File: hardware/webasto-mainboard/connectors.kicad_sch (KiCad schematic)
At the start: 5 parts

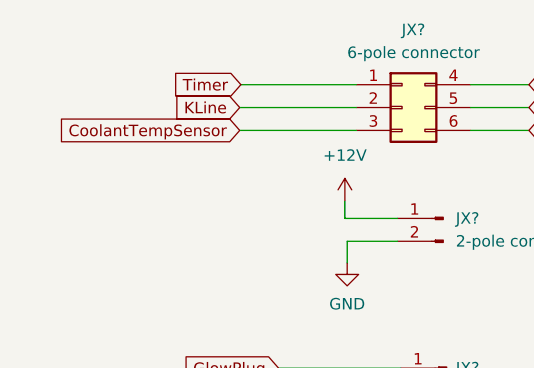
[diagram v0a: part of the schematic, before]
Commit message: Update schematics.  Had a better idea.
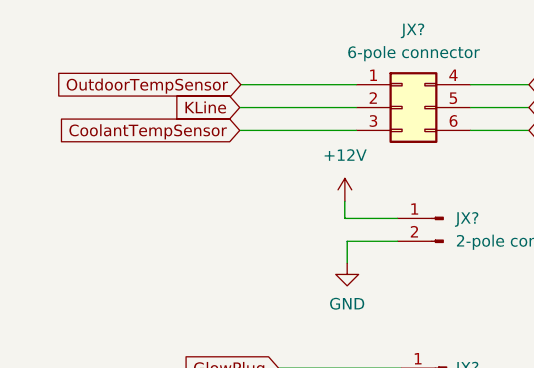
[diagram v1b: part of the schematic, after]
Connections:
- net Timer renamed OutdoorTempSensor
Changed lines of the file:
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@@
     )
   )
-  (global_label "Timer" (shape input) (at 127.508 58.166 180) (fields_autoplaced)
+  (global_label "OutdoorTempSensor" (shape input) (at 127.508 58.166 180) (fields_autoplaced)
     (effects (font (size 1.27 1.27)) (justify right))
-    (property "Intersheet References" "${INTERSHEET_REFS}" (id 0) (at 119.9544 58.0866 0)
+    (property "Intersheet References" "${INTERSHEET_REFS}" (id 0) (at 106.3473 58.0866 0)
       (effects (font (size 1.27 1.27)) (justify right) hide)
     )

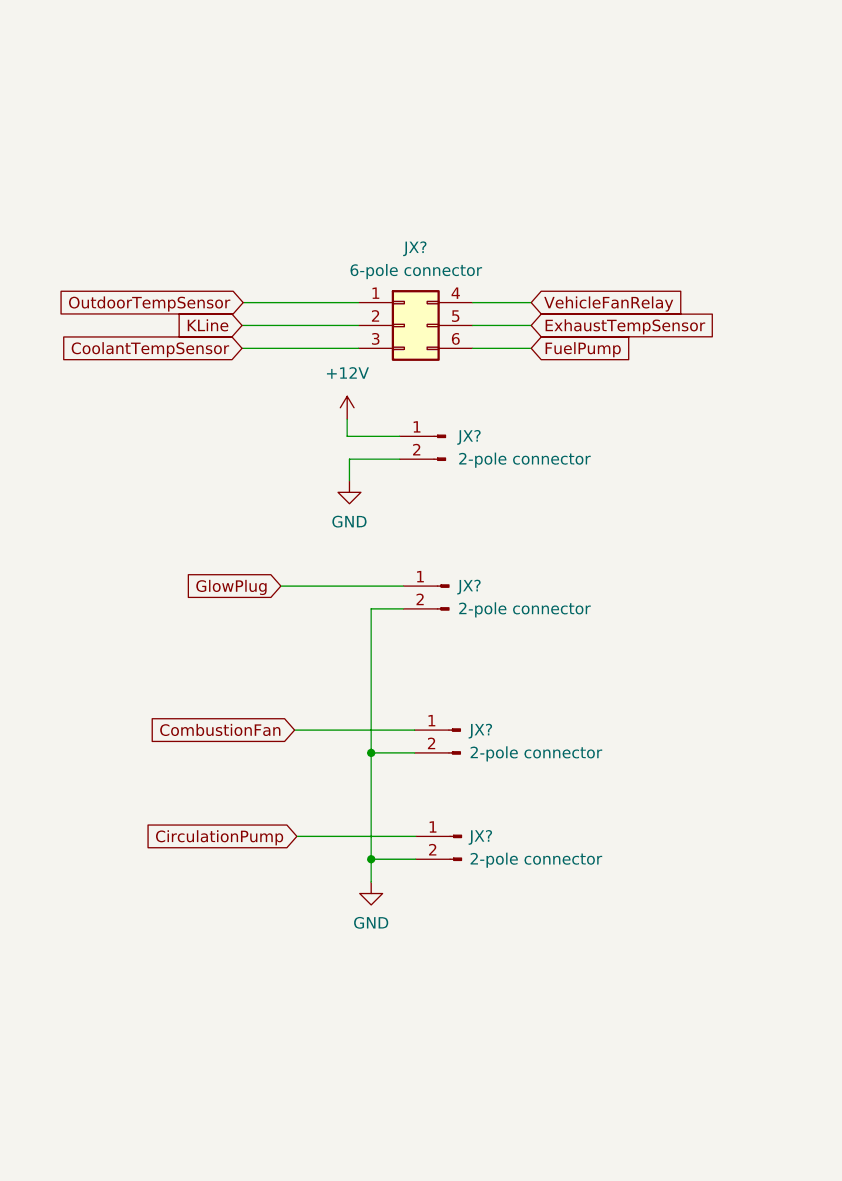
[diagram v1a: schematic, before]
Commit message: Split out the sensor board for analog sensors
- Talks to the controller via I2C over a QWIIC chain.
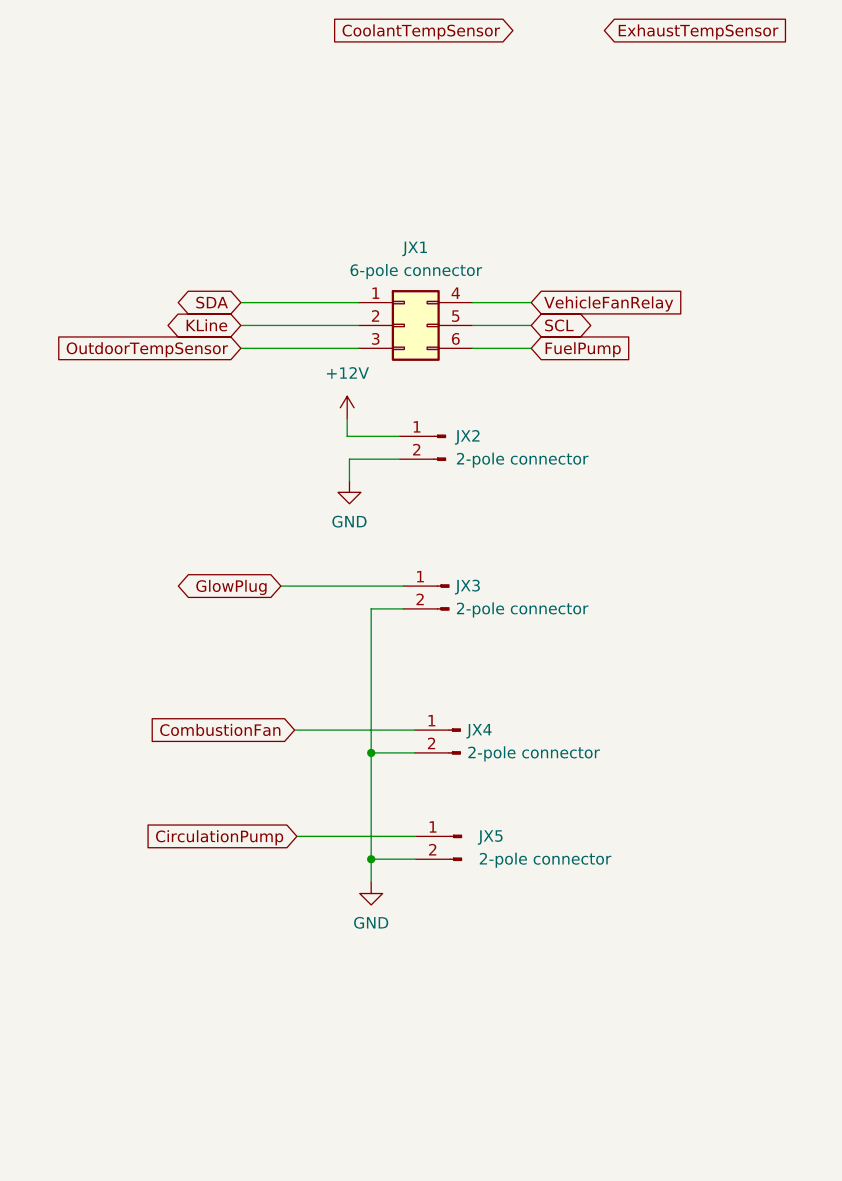
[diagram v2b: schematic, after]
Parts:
- gave numbers to parts that had none: 5
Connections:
- net CoolantTempSensor: no longer JX1.3 (Pin_3)
- net ExhaustTempSensor: no longer JX1.5 (Pin_5)
- net OutdoorTempSensor: now also JX1.3 (Pin_3); no longer JX1.1 (Pin_1)
- new net SCL: JX1.5 (Pin_5)
- new net SDA: JX1.1 (Pin_1)
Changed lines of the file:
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@@
     (stroke (width 0) (type default) (color 0 0 0 0))
   )
-  (wire (pts (xy 127.381 63.246) (xy 140.335 63.246))
+  (wire (pts (xy 127.254 63.246) (xy 140.335 63.246))
     (stroke (width 0) (type default) (color 0 0 0 0))
   )
-  (wire (pts (xy 127.508 58.166) (xy 140.335 58.166))
+  (wire (pts (xy 127.254 58.166) (xy 140.335 58.166))
     (stroke (width 0) (type default) (color 0 0 0 0))
   )
@@
     (stroke (width 0) (type default) (color 0 0 0 0))
   )
-  (wire (pts (xy 127.381 60.706) (xy 140.335 60.706))
+  (wire (pts (xy 127.254 60.706) (xy 140.335 60.706))
     (stroke (width 0) (type default) (color 0 0 0 0))
   )
@@
     )
   )
-  (global_label "KLine" (shape input) (at 127.381 60.706 180) (fields_autoplaced)
+  (global_label "KLine" (shape bidirectional) (at 127.254 60.706 180) (fields_autoplaced)
     (effects (font (size 1.27 1.27)) (justify right))
-    (property "Intersheet References" "${INTERSHEET_REFS}" (id 0) (at 119.8274 60.6266 0)
+    (property "Intersheet References" "${INTERSHEET_REFS}" (id 0) (at 119.7004 60.6266 0)
+      (effects (font (size 1.27 1.27)) (justify right) hide)
+    )
+  )
+  (global_label "SDA" (shape bidirectional) (at 127.254 58.166 180) (fields_autoplaced)
+    (effects (font (size 1.27 1.27)) (justify right))
+    (property "Intersheet References" "${INTERSHEET_REFS}" (id 0) (at 121.2728 58.0866 0)
       (effects (font (size 1.27 1.27)) (justify right) hide)
     )
@@
     )
   )
-  (global_label "ExhaustTempSensor" (shape input) (at 159.512 60.706 0) (fields_autoplaced)
+  (global_label "SCL" (shape bidirectional) (at 159.512 60.706 0) (fields_autoplaced)
     (effects (font (size 1.27 1.27)) (justify left))
-    (property "Intersheet References" "${INTERSHEET_REFS}" (id 0) (at 180.6122 60.6266 0)
+    (property "Intersheet References" "${INTERSHEET_REFS}" (id 0) (at 165.4327 60.6266 0)
+      (effects (font (size 1.27 1.27)) (justify left) hide)
+    )
+  )
+  (global_label "ExhaustTempSensor" (shape input) (at 167.64 27.94 0) (fields_autoplaced)
+    (effects (font (size 1.27 1.27)) (justify left))
+    (property "Intersheet References" "${INTERSHEET_REFS}" (id 0) (at 188.7402 27.8606 0)
       (effects (font (size 1.27 1.27)) (justify left) hide)
     )
@@
     )
   )
-  (global_label "GlowPlug" (shape input) (at 131.699 89.662 180) (fields_autoplaced)
+  (global_label "GlowPlug" (shape bidirectional) (at 131.699 89.662 180) (fields_autoplaced)
     (effects (font (size 1.27 1.27)) (justify right))
     (property "Intersheet References" "${INTERSHEET_REFS}" (id 0) (at 120.6378 89.5826 0)
@@
     )
   )
-  (global_label "OutdoorTempSensor" (shape input) (at 127.508 58.166 180) (fields_autoplaced)
+  (global_label "OutdoorTempSensor" (shape input) (at 127.254 63.246 180) (fields_autoplaced)
     (effects (font (size 1.27 1.27)) (justify right))
-    (property "Intersheet References" "${INTERSHEET_REFS}" (id 0) (at 106.3473 58.0866 0)
+    (property "Intersheet References" "${INTERSHEET_REFS}" (id 0) (at 106.0933 63.1666 0)
       (effects (font (size 1.27 1.27)) (justify right) hide)
     )
   )
-  (global_label "CoolantTempSensor" (shape input) (at 127.381 63.246 180) (fields_autoplaced)
+  (global_label "CoolantTempSensor" (shape input) (at 157.48 27.94 180) (fields_autoplaced)
     (effects (font (size 1.27 1.27)) (justify right))
-    (property "Intersheet References" "${INTERSHEET_REFS}" (id 0) (at 106.4017 63.1666 0)
+    (property "Intersheet References" "${INTERSHEET_REFS}" (id 0) (at 136.5007 27.8606 0)
       (effects (font (size 1.27 1.27)) (justify right) hide)
     )
@@
   (symbol (lib_id "Connector_Generic:Conn_02x03_Top_Bottom") (at 145.415 60.706 0) (unit 1)
     (in_bom yes) (on_board yes) (fields_autoplaced)
-    (property "Reference" "JX?" (id 0) (at 146.685 52.07 0))
+    (property "Reference" "JX1" (id 0) (at 146.685 52.07 0))
     (property "Value" "6-pole connector" (id 1) (at 146.685 54.61 0))
     (property "Footprint" "" (id 2) (at 145.415 60.706 0)
@@
   (symbol (lib_id "Connector:Conn_01x02_Male") (at 151.638 105.664 0) (mirror y) (unit 1)
     (in_bom yes) (on_board yes) (fields_autoplaced)
-    (property "Reference" "JX?" (id 0) (at 152.654 105.6639 0)
+    (property "Reference" "JX4" (id 0) (at 152.4 105.6639 0)
       (effects (font (size 1.27 1.27)) (justify right))
     )
-    (property "Value" "2-pole connector" (id 1) (at 152.654 108.2039 0)
+    (property "Value" "2-pole connector" (id 1) (at 152.4 108.2039 0)
       (effects (font (size 1.27 1.27)) (justify right))
     )
@@
   (symbol (lib_id "Connector:Conn_01x02_Male") (at 151.765 117.475 0) (mirror y) (unit 1)
     (in_bom yes) (on_board yes) (fields_autoplaced)
-    (property "Reference" "JX?" (id 0) (at 152.654 117.4749 0)
+    (property "Reference" "JX5" (id 0) (at 153.67 117.4749 0)
       (effects (font (size 1.27 1.27)) (justify right))
     )
-    (property "Value" "2-pole connector" (id 1) (at 152.654 120.0149 0)
+    (property "Value" "2-pole connector" (id 1) (at 153.67 120.0149 0)
       (effects (font (size 1.27 1.27)) (justify right))
     )
@@
   (symbol (lib_id "Connector:Conn_01x02_Male") (at 150.368 89.662 0) (mirror y) (unit 1)
     (in_bom yes) (on_board yes) (fields_autoplaced)
-    (property "Reference" "JX?" (id 0) (at 151.384 89.6619 0)
+    (property "Reference" "JX3" (id 0) (at 151.13 89.6619 0)
       (effects (font (size 1.27 1.27)) (justify right))
     )
-    (property "Value" "2-pole connector" (id 1) (at 151.384 92.2019 0)
+    (property "Value" "2-pole connector" (id 1) (at 151.13 92.2019 0)
       (effects (font (size 1.27 1.27)) (justify right))
     )
@@
   (symbol (lib_id "Connector:Conn_01x02_Male") (at 149.987 73.025 0) (mirror y) (unit 1)
     (in_bom yes) (on_board yes) (fields_autoplaced)
-    (property "Reference" "JX?" (id 0) (at 151.384 73.0249 0)
+    (property "Reference" "JX2" (id 0) (at 151.13 73.0249 0)
       (effects (font (size 1.27 1.27)) (justify right))
     )
-    (property "Value" "2-pole connector" (id 1) (at 151.384 75.5649 0)
+    (property "Value" "2-pole connector" (id 1) (at 151.13 75.5649 0)
       (effects (font (size 1.27 1.27)) (justify right))
     )

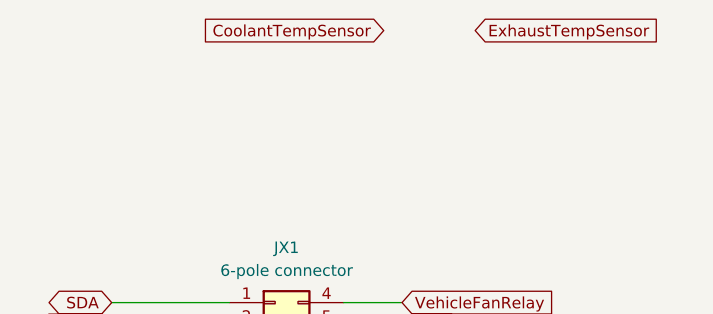
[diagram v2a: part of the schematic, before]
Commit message: Added QWIIC Interface schematic, more cleanup
- redid all the MOSFET drives.  The fan one still concerns me a bit.
  is it supposed to DRIVE a relay, or BE a relay?  As long as it's a 12V
  relay, we should be good.
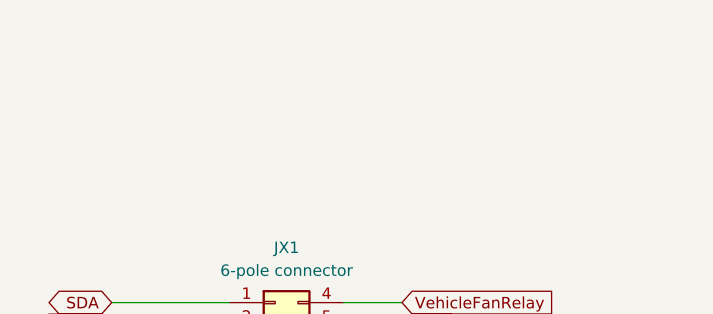
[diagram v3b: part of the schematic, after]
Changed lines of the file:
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@@
-    )
-  )
-  (global_label "ExhaustTempSensor" (shape input) (at 167.64 27.94 0) (fields_autoplaced)
-    (effects (font (size 1.27 1.27)) (justify left))
-    (property "Intersheet References" "${INTERSHEET_REFS}" (id 0) (at 188.7402 27.8606 0)
-      (effects (font (size 1.27 1.27)) (justify left) hide)
     )
   )
@@
       (effects (font (size 1.27 1.27)) (justify right) hide)
     )
-  )
-  (global_label "CoolantTempSensor" (shape input) (at 157.48 27.94 180) (fields_autoplaced)
-    (effects (font (size 1.27 1.27)) (justify right))
-    (property "Intersheet References" "${INTERSHEET_REFS}" (id 0) (at 136.5007 27.8606 0)
-      (effects (font (size 1.27 1.27)) (justify right) hide)
-    )

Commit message: v1.0 layout complete
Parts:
- added F1: 6A Polyfuse, Resistor_SMD:R_0603_1608Metric_Pad0.98x0.95mm_HandSolder, symbol Device:Polyfuse
- JX1: footprint (none) -> Beirdo:Webasto_Therma_Top_C_X1
- JX2: footprint (none) -> Beirdo:Webasto_Therma_Top_C_X2
- JX3: footprint (none) -> Beirdo:Webasto_Therma_Top_C_X3
- JX4, JX5: footprint (none) -> Beirdo:Webasto_Therma_Top_C_X4X5
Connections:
- net OutdoorTempSensor is gone; now on net SDA: JX1.3 (Pin_3)
- net +12V: now also F1.1; no longer JX2.1 (Pin_1)
- net GND: no longer JX3.2 (Pin_2)
- net SDA: no longer JX1.1 (Pin_1)
- net GlowPlug renamed GlowPlug+
- new net: F1.2, JX2.1 (Pin_1)
- new net GlowPlug-: JX3.2 (Pin_2)
- new net StartRun: JX1.1 (Pin_1)

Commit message: Added title block info
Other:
- title: (none) -> Webasto Thermo Top C Replacement Controller
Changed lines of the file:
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@@
 (kicad_sch (version 20211123) (generator eeschema)
   (paper "A4")
+  (title_block
+    (title "Webasto Thermo Top C Replacement Controller")
+    (date "2023-01-19")
+    (rev "v1.0")
+  )
   (junction (at 141.732 120.015) (diameter 0) (color 0 0 0 0)
   )

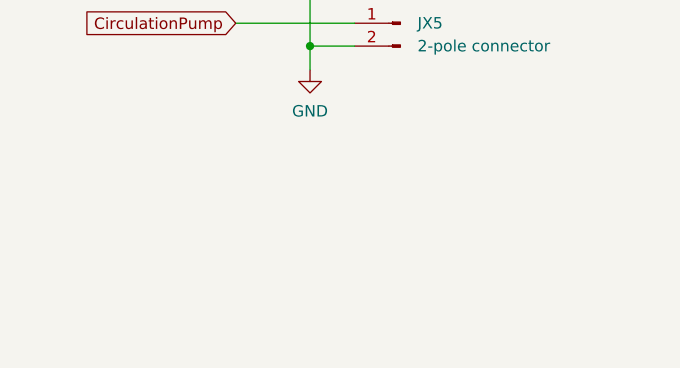
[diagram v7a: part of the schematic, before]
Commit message: Added EmergencyStop input.  Hope I never need it.
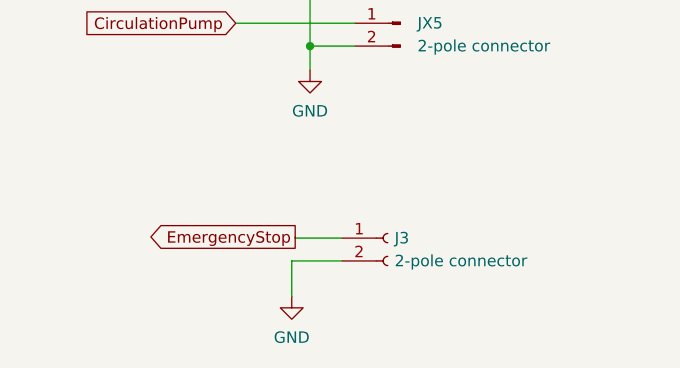
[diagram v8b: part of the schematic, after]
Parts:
- added J3: 2-pole connector, Connector_PinHeader_2.54mm:PinHeader_1x02_P2.54mm_Horizontal, symbol Connector:Conn_01x02_Female
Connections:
- net GND: now also J3.2 (Pin_2)
- new net EmergencyStop: J3.1 (Pin_1)
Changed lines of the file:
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@@
+    (stroke (width 0) (type default) (color 0 0 0 0))
+  )
+  (wire (pts (xy 139.7 143.891) (xy 145.288 143.891))
     (stroke (width 0) (type default) (color 0 0 0 0))
   )
@@
     (stroke (width 0) (type default) (color 0 0 0 0))
   )
+  (wire (pts (xy 139.7 143.891) (xy 139.7 147.828))
+    (stroke (width 0) (type default) (color 0 0 0 0))
+  )
   (wire (pts (xy 153.035 58.166) (xy 159.512 58.166))
     (stroke (width 0) (type default) (color 0 0 0 0))
   )
+  (wire (pts (xy 145.288 141.351) (xy 140.081 141.351))
+    (stroke (width 0) (type default) (color 0 0 0 0))
+  )
   (wire (pts (xy 133.477 117.475) (xy 146.685 117.475))
     (stroke (width 0) (type default) (color 0 0 0 0))
@@
   )
   (wire (pts (xy 133.858 73.025) (xy 144.907 73.025))
+    (stroke (width 0) (type default) (color 0 0 0 0))
+  )
+  (wire (pts (xy 140.081 141.351) (xy 140.081 141.224))
     (stroke (width 0) (type default) (color 0 0 0 0))
   )
@@
     (property "Intersheet References" "${INTERSHEET_REFS}" (id 0) (at 171.178 63.1666 0)
       (effects (font (size 1.27 1.27)) (justify left) hide)
+    )
+  )
+  (global_label "EmergencyStop" (shape output) (at 140.081 141.224 180) (fields_autoplaced)
+    (effects (font (size 1.27 1.27)) (justify right))
+    (property "Intersheet References" "${INTERSHEET_REFS}" (id 0) (at 123.2746 141.1446 0)
+      (effects (font (size 1.27 1.27)) (justify right) hide)
     )
   )
@@
   (symbol (lib_id "power:GND") (at 141.732 122.682 0) (unit 1)
     (in_bom yes) (on_board yes) (fields_autoplaced)
-    (property "Reference" "#PWR017" (id 0) (at 141.732 129.032 0)
+    (property "Reference" "#PWR018" (id 0) (at 141.732 129.032 0)
       (effects (font (size 1.27 1.27)) hide)
     )
@@
       (effects (font (size 1.27 1.27)) hide)
     )
+    (pin "1")
+  )
+  (symbol (lib_id "Connector:Conn_01x02_Female") (at 150.368 141.351 0) (unit 1)
+    (in_bom yes) (on_board yes) (fields_autoplaced)
+    (property "Reference" "J3" (id 0) (at 151.13 141.3509 0)
+      (effects (font (size 1.27 1.27)) (justify left))
+    )
+    (property "Value" "2-pole connector" (id 1) (at 151.13 143.8909 0)
+      (effects (font (size 1.27 1.27)) (justify left))
+    )
+    (property "Footprint" "Connector_PinHeader_2.54mm:PinHeader_1x02_P2.54mm_Horizontal" (id 2) (at 150.368 141.351 0)
+      (effects (font (size 1.27 1.27)) hide)
+    )
+    (property "Datasheet" "~" (id 3) (at 150.368 141.351 0)
+      (effects (font (size 1.27 1.27)) hide)
+    )
+    (pin "1")
+    (pin "2")
+  )
+  (symbol (lib_id "power:GND") (at 139.7 147.828 0) (unit 1)
+    (in_bom yes) (on_board yes) (fields_autoplaced)
+    (property "Reference" "#PWR017" (id 0) (at 139.7 154.178 0)
+      (effects (font (size 1.27 1.27)) hide)
+    )
+    (property "Value" "GND" (id 1) (at 139.7 152.4 0))
+    (property "Footprint" "" (id 2) (at 139.7 147.828 0)
+      (effects (font (size 1.27 1.27)) hide)
+    )
+    (property "Datasheet" "" (id 3) (at 139.7 147.828 0)
+      (effects (font (size 1.27 1.27)) hide)
+    )
